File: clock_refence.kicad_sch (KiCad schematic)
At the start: 52 parts, among them J204 REFOUT_AUX_P, J205 REFOUT_AUX_N, J206 RFShield_TwoPieces, J207 REFOUT, J209 DNP, T202 TC2-1T+, U201 Si53301, U202 XC6204B33

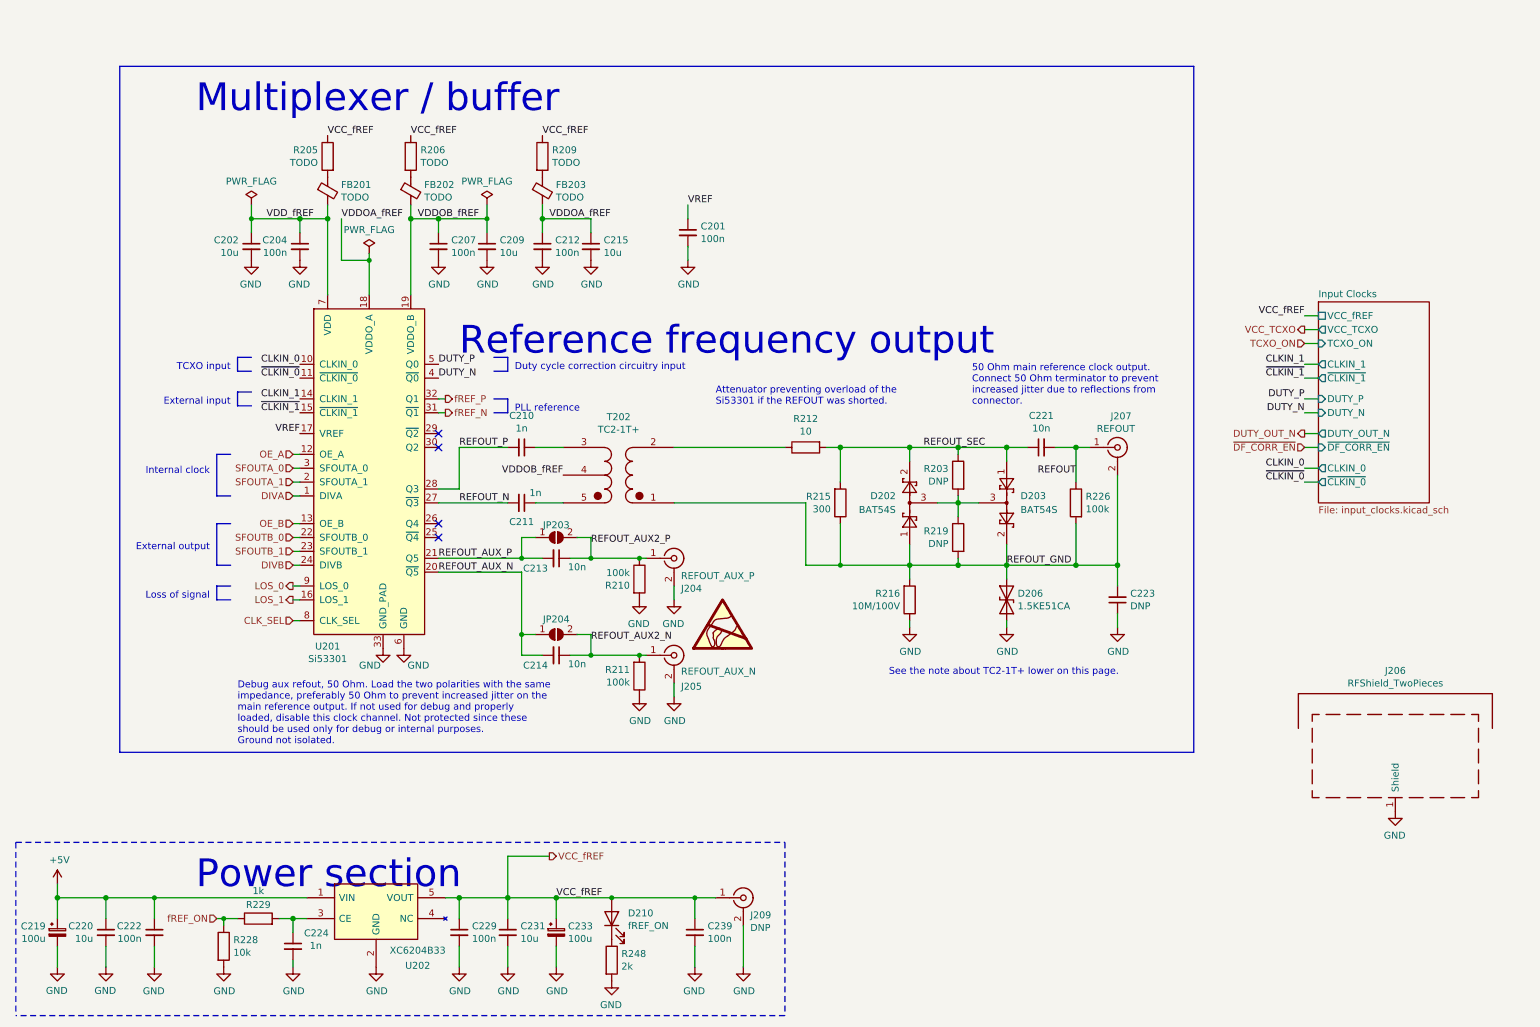
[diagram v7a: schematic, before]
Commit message: Resolved all broken symbols / packages / links except TCXO.
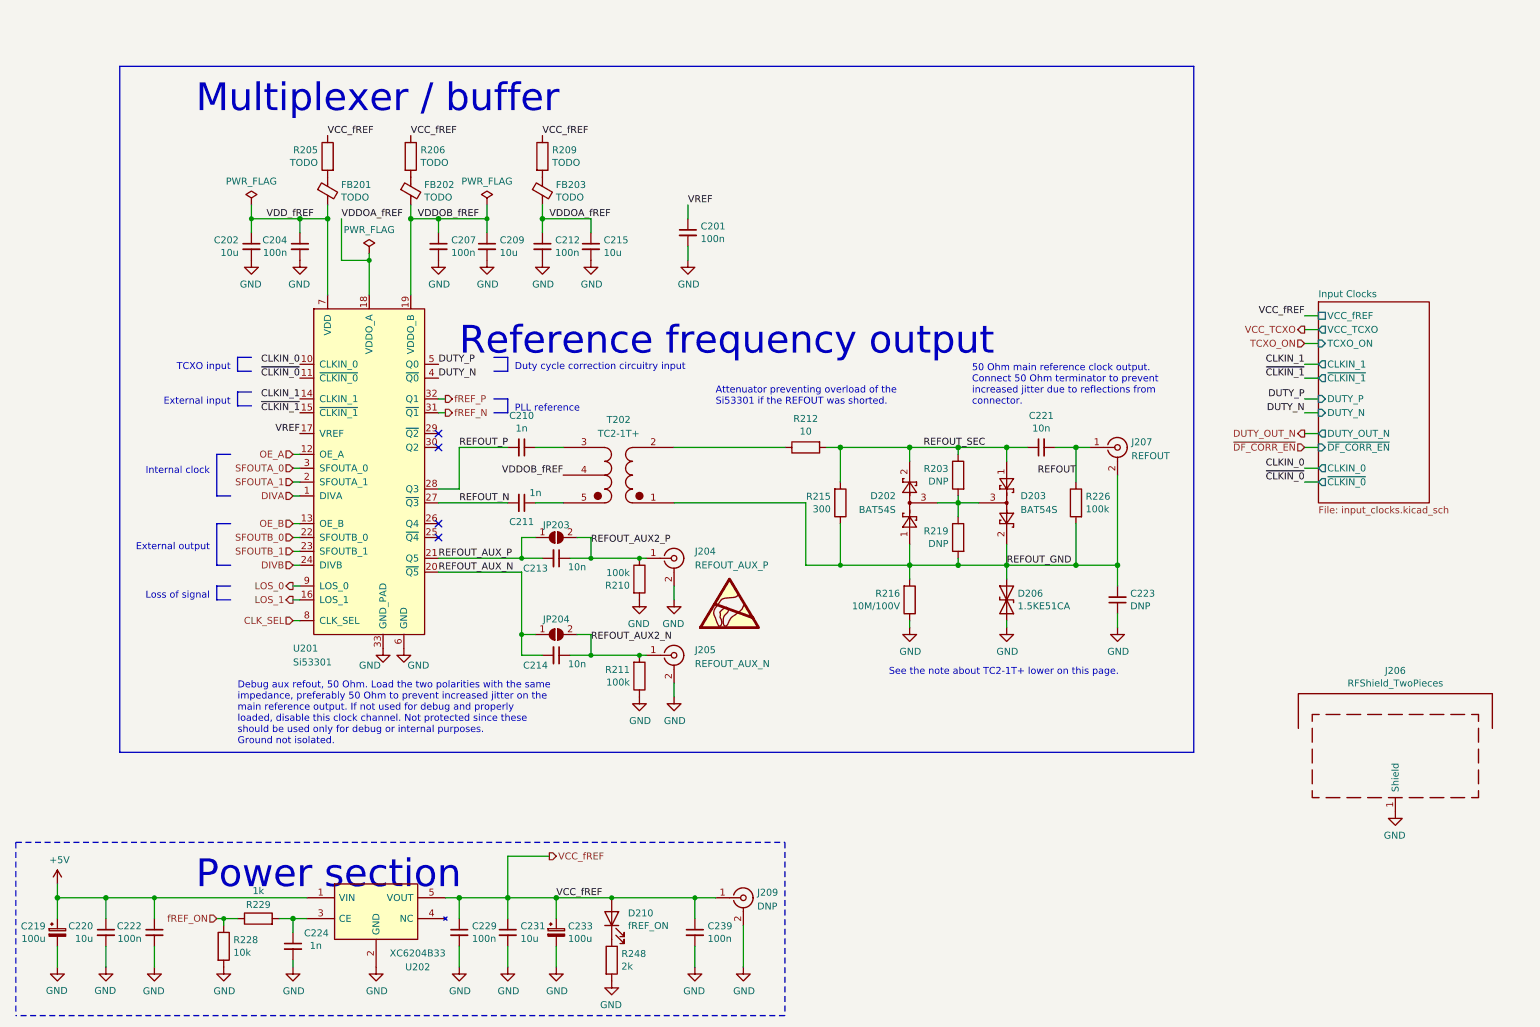
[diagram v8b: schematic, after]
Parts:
- removed J204: REFOUT_AUX_P, Connector_Coaxial:U.FL_Molex_MCRF_73412-0110_Vertical, symbol Connector:Conn_Coaxial
- removed J205: REFOUT_AUX_N, Connector_Coaxial:U.FL_Molex_MCRF_73412-0110_Vertical, symbol Connector:Conn_Coaxial
- removed J207: REFOUT, petr_kicad:SMA_rosenberger_hybrid, symbol Connector:Conn_Coaxial
- removed J209: DNP, Connector_Coaxial:U.FL_Molex_MCRF_73412-0110_Vertical, symbol Connector:Conn_Coaxial
- removed T202: TC2-1T+, Transformer_SMD:Transformer_MACOM_SM-22, symbol petr_lib_nightly:TC2-1T+
- removed U201: Si53301, petr_kicad:QFN-32_EP_5x5_Pitch0.5mm_Si53301, symbol petr_lib_nightly:Si53301
- removed U202: XC6204B33, Package_TO_SOT_SMD:SOT-89-5_Handsoldering, symbol petr_lib_nightly:XC6204B33
- added J204: REFOUT_AUX_P, Connector_Coaxial:U.FL_Molex_MCRF_73412-0110_Vertical, symbol petr:u.FL
- added J205: REFOUT_AUX_N, Connector_Coaxial:U.FL_Molex_MCRF_73412-0110_Vertical, symbol petr:u.FL
- added J207: REFOUT, petr_kicad:SMA_rosenberger_hybrid, symbol petr:SMA_Rosenberger_32K243-40ML5_chinese_SMA_hybrid
- added J209: DNP, Connector_Coaxial:U.FL_Molex_MCRF_73412-0110_Vertical, symbol petr:u.FL
- added T202: TC2-1T+, petr:Transformer_MiniCircuits_AT224-1A, symbol petr:TC2-1T+
- added U201: Si53301, petr:QFN-32_EP_5x5_Pitch0.5mm_Si53301, symbol petr:Si53301
- added U202: XC6204B33, Package_TO_SOT_SMD:SOT-89-5_Handsoldering, symbol petr:XC6204B33
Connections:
- net +5V: now also U202.1 (VIN)
- net CLKIN_0: now also U201.10 (CLKIN_0)
- net CLKIN_1: now also U201.14 (CLKIN_1)
- net CLK_SEL: now also U201.8 (CLK_SEL)
- net DIVA: now also U201.1 (DIVA)
- net DIVB: now also U201.24 (DIVB)
- net DUTY_N: now also U201.4 (~{Q0})
- net DUTY_P: now also U201.5 (Q0)
- net GND: now also J204.2 (Ext), J205.2 (Ext), J209.2 (Ext), U201.33 (GND_PAD), U201.6 (GND), U202.2 (GND)
- net LOS_0: now also U201.9 (LOS_0)
- net LOS_1: now also U201.16 (LOS_1)
- net OE_A: now also U201.12 (OE_A)
- net OE_B: now also U201.13 (OE_B)
- net REFOUT: now also J207.1 (In)
- net REFOUT_AUX2_N: now also J205.1 (In)
- net REFOUT_AUX2_P: now also J204.1 (In)
- net REFOUT_AUX_N: now also U201.20 (~{Q5})
- net REFOUT_AUX_P: now also U201.21 (Q5)
- net REFOUT_GND: now also J207.2 (Ext), T202.1 (AA)
- net REFOUT_N: now also U201.27 (~{Q3})
- net REFOUT_P: now also U201.28 (Q3)
- net SFOUTA_0: now also U201.3 (SFOUTA_0)
- net SFOUTA_1: now also U201.2 (SFOUTA_1)
- net SFOUTB_0: now also U201.22 (SFOUTB_0)
- net SFOUTB_1: now also U201.23 (SFOUTB_1)
- net VCC_fREF: now also J209.1 (In), U202.5 (VOUT)
- net VDDOA_fREF: now also U201.18 (VDDO_A)
- net VDDOB_fREF: now also T202.4 (SC), U201.19 (VDDO_B)
- net VDD_fREF: now also U201.7 (VDD)
- net VREF: now also U201.17 (VREF)
- net fREF_N: now also U201.31 (~{Q1})
- net fREF_P: now also U201.32 (Q1)
- net ~{CLKIN_0}: now also U201.11 (~{CLKIN_0})
- net ~{CLKIN_1}: now also U201.15 (~{CLKIN_1})
- net at C210.1: now also T202.3 (SA)
- net at C211.1: now also T202.5 (SB)
- net at R212.1: now also T202.2 (AB)
- net at C224.1, R229.2: now also U202.3 (CE)
